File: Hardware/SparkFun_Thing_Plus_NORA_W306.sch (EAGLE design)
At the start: 76 parts, among them J1 THING_PLUS_LOGICAL, J2 LiPo, J3 QWIIC_RA, J4 MICRO-SDFRICTION, J5 USB-C, J6 SWD, Q1 3.1A/30V/105mΩ, Q2 MBT3904DW1T1, U1 UBLOX_NORA_W306, U3 XC6222B331MR-G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

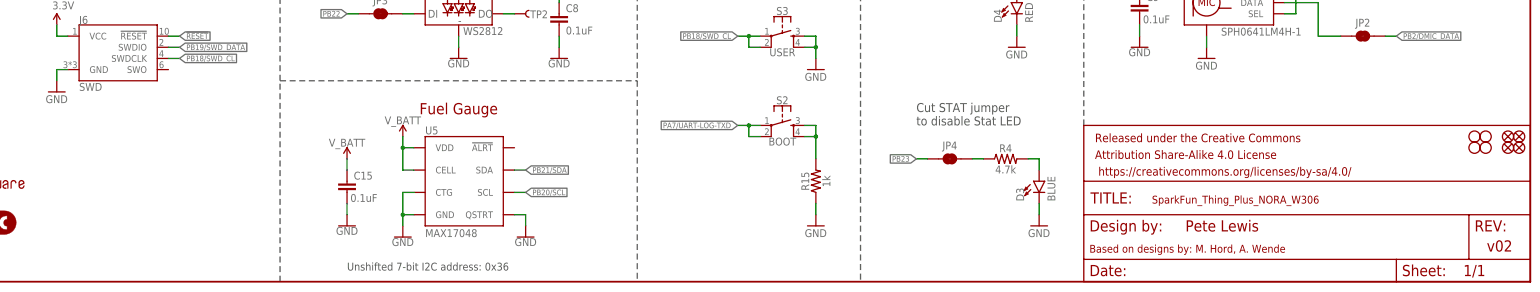
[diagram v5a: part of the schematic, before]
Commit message: SWD header to DNP and bumped version to v03
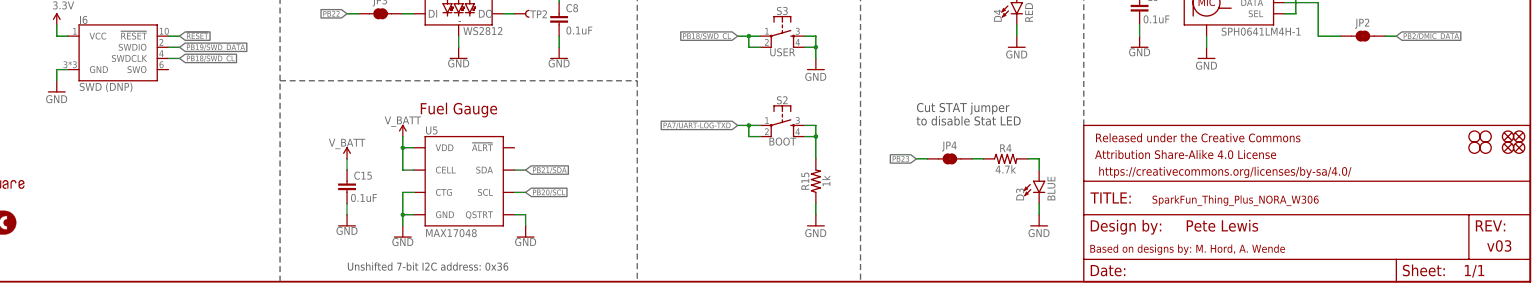
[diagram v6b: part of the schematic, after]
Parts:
- J6: value SWD -> SWD (DNP)
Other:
- note added: "v03"
- note removed: "v02"
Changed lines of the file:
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@@
 <part name="C11" library="SparkFun-Capacitors" deviceset="0.1UF" device="-0402T-16V-10%" value="0.1uF"/>
 <part name="GND7" library="SparkFun-PowerSymbols" deviceset="GND" device=""/>
-<part name="J6" library="SparkFun-Connectors" deviceset="CORTEX_JTAG_DEBUG_MINIMUM" device="_SMD-UNSHROUDED" value="SWD"/>
+<part name="J6" library="SparkFun-Connectors" deviceset="CORTEX_JTAG_DEBUG_MINIMUM" device="_SMD-UNSHROUDED" value="SWD (DNP)"/>
 <part name="SUPPLY31" library="SparkFun-PowerSymbols" deviceset="3.3V" device=""/>
 <part name="GND33" library="SparkFun-PowerSymbols" deviceset="GND" device=""/>
@@
 <text x="73.66" y="175.26" size="2.54" layer="94" font="vector" align="bottom-center">u-blox NORA-W306 Module</text>
 <text x="182.88" y="175.26" size="2.54" layer="94" font="vector" align="bottom-center">Thing Plus Headers</text>
-<text x="421.894" y="9.398" size="2.54" layer="94" font="vector" align="top-left">v02</text>
+<text x="421.894" y="9.398" size="2.54" layer="94" font="vector" align="top-left">v03</text>
 <text x="391.16" y="175.26" size="2.54" layer="94" font="vector" align="bottom-center">QWIIC Connector &amp; I2C Pullups</text>
 <text x="353.314" y="11.43" size="2.54" layer="94" font="vector">Pete Lewis</text>

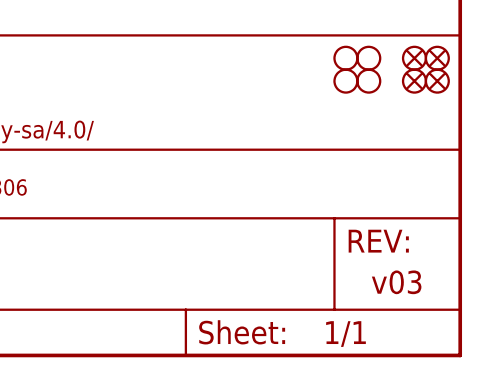
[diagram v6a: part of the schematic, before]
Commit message: removed paste from cortex debug SMD footprint (DNP)
-also bumped version to v04
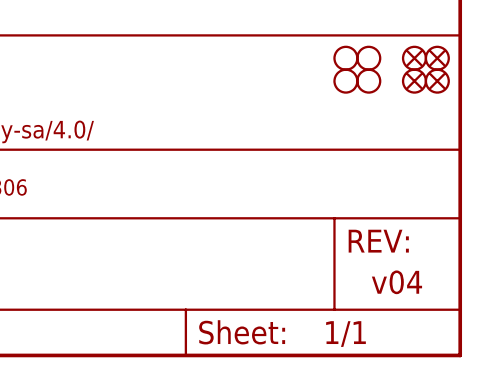
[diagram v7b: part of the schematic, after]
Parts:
- J6: device SparkFun-Connectors:CORTEX_JTAG_DEBUG_MINIMUM_SMD-UNSHROUDED -> SparkFun-Connectors:CORTEX_JTAG_DEBUG_MINIMUM_SMD_UNSHROUDED_DNP_NO_PASTE
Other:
- note added: "v04"
- note removed: "v03"
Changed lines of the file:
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@@
 <grid distance="0.1" unitdist="inch" unit="inch" style="lines" multiple="1" display="no" altdistance="0.01" altunitdist="inch" altunit="inch"/>
 <layers>
-<layer number="1" name="Top" color="4" fill="1" visible="no" active="no"/>
-<layer number="2" name="Route2" color="1" fill="3" visible="no" active="no"/>
-<layer number="3" name="Route3" color="4" fill="3" visible="no" active="no"/>
-<layer number="4" name="Route4" color="1" fill="4" visible="no" active="no"/>
-<layer number="5" name="Route5" color="4" fill="4" visible="no" active="no"/>
-<layer number="6" name="Route6" color="1" fill="8" visible="no" active="no"/>
-<layer number="7" name="Route7" color="4" fill="8" visible="no" active="no"/>
-<layer number="8" name="Route8" color="1" fill="2" visible="no" active="no"/>
-<layer number="9" name="Route9" color="4" fill="2" visible="no" active="no"/>
-<layer number="10" name="Route10" color="1" fill="7" visible="no" active="no"/>
-<layer number="11" name="Route11" color="4" fill="7" visible="no" active="no"/>
-<layer number="12" name="Route12" color="1" fill="5" visible="no" active="no"/>
-<layer number="13" name="Route13" color="4" fill="5" visible="no" active="no"/>
-<layer number="14" name="Route14" color="1" fill="6" visible="no" active="no"/>
-<layer number="15" name="Route15" color="11" fill="6" visible="no" active="no"/>
-<layer number="16" name="Bottom" color="1" fill="1" visible="no" active="no"/>
-<layer number="17" name="Pads" color="2" fill="1" visible="no" active="no"/>
-<layer number="18" name="Vias" color="2" fill="1" visible="no" active="no"/>
-<layer number="19" name="Unrouted" color="6" fill="1" visible="no" active="no"/>
-<layer number="20" name="Dimension" color="24" fill="1" visible="no" active="no"/>
-<layer number="21" name="tPlace" color="16" fill="1" visible="no" active="no"/>
-<layer number="22" name="bPlace" color="14" fill="1" visible="no" active="no"/>
-<layer number="23" name="tOrigins" color="15" fill="1" visible="no" active="no"/>
-<layer number="24" name="bOrigins" color="15" fill="1" visible="no" active="no"/>
-<layer number="25" name="tNames" color="7" fill="1" visible="no" active="no"/>
-<layer number="26" name="bNames" color="7" fill="1" visible="no" active="no"/>
-<layer number="27" name="tValues" color="7" fill="1" visible="no" active="no"/>
-<layer number="28" name="bValues" color="7" fill="1" visible="no" active="no"/>
+<layer number="1" name="Top" color="4" fill="1" visible="yes" active="no"/>
+<layer number="2" name="Route2" color="1" fill="3" visible="yes" active="no"/>
+<layer number="3" name="Route3" color="4" fill="3" visible="yes" active="no"/>
+<layer number="4" name="Route4" color="1" fill="4" visible="yes" active="no"/>
+<layer number="5" name="Route5" color="4" fill="4" visible="yes" active="no"/>
+<layer number="6" name="Route6" color="1" fill="8" visible="yes" active="no"/>
+<layer number="7" name="Route7" color="4" fill="8" visible="yes" active="no"/>
+<layer number="8" name="Route8" color="1" fill="2" visible="yes" active="no"/>
+<layer number="9" name="Route9" color="4" fill="2" visible="yes" active="no"/>
+<layer number="10" name="Route10" color="1" fill="7" visible="yes" active="no"/>
+<layer number="11" name="Route11" color="4" fill="7" visible="yes" active="no"/>
+<layer number="12" name="Route12" color="1" fill="5" visible="yes" active="no"/>
+<layer number="13" name="Route13" color="4" fill="5" visible="yes" active="no"/>
+<layer number="14" name="Route14" color="1" fill="6" visible="yes" active="no"/>
+<layer number="15" name="Route15" color="11" fill="6" visible="yes" active="no"/>
+<layer number="16" name="Bottom" color="1" fill="1" visible="yes" active="no"/>
+<layer number="17" name="Pads" color="2" fill="1" visible="yes" active="no"/>
+<layer number="18" name="Vias" color="2" fill="1" visible="yes" active="no"/>
+<layer number="19" name="Unrouted" color="6" fill="1" visible="yes" active="no"/>
+<layer number="20" name="Dimension" color="24" fill="1" visible="yes" active="no"/>
+<layer number="21" name="tPlace" color="16" fill="1" visible="yes" active="no"/>
+<layer number="22" name="bPlace" color="14" fill="1" visible="yes" active="no"/>
+<layer number="23" name="tOrigins" color="15" fill="1" visible="yes" active="no"/>
+<layer number="24" name="bOrigins" color="15" fill="1" visible="yes" active="no"/>
+<layer number="25" name="tNames" color="7" fill="1" visible="yes" active="no"/>
+<layer number="26" name="bNames" color="7" fill="1" visible="yes" active="no"/>
+<layer number="27" name="tValues" color="7" fill="1" visible="yes" active="no"/>
+<layer number="28" name="bValues" color="7" fill="1" visible="yes" active="no"/>
 <layer number="29" name="tStop" color="7" fill="3" visible="no" active="no"/>
 <layer number="30" name="bStop" color="7" fill="6" visible="no" active="no"/>
@@
 <layer number="35" name="tGlue" color="7" fill="4" visible="no" active="no"/>
 <layer number="36" name="bGlue" color="7" fill="5" visible="no" active="no"/>
-<layer number="37" name="tTest" color="7" fill="1" visible="no" active="no"/>
-<layer number="38" name="bTest" color="7" fill="1" visible="no" active="no"/>
+<layer number="37" name="tTest" color="7" fill="1" visible="yes" active="no"/>
+<layer number="38" name="bTest" color="7" fill="1" visible="yes" active="no"/>
 <layer number="39" name="tKeepout" color="4" fill="11" visible="no" active="no"/>
 <layer number="40" name="bKeepout" color="1" fill="11" visible="no" active="no"/>
@@
 <layer number="44" name="Drills" color="7" fill="1" visible="no" active="no"/>
 <layer number="45" name="Holes" color="7" fill="1" visible="no" active="no"/>
-<layer number="46" name="Milling" color="3" fill="1" visible="no" active="no"/>
-<layer number="47" name="Measures" color="7" fill="1" visible="no" active="no"/>
-<layer number="48" name="Document" color="7" fill="1" visible="no" active="no"/>
-<layer number="49" name="Reference" color="7" fill="1" visible="no" active="no"/>
-<layer number="50" name="dxf" color="7" fill="1" visible="no" active="no"/>
-<layer number="51" name="tDocu" color="6" fill="1" visible="no" active="no"/>
-<layer number="52" name="bDocu" color="7" fill="1" visible="no" active="no"/>
-<layer number="53" name="tGND_GNDA" color="7" fill="9" visible="no" active="no"/>
-<layer number="54" name="bGND_GNDA" color="1" fill="9" visible="no" active="no"/>
-<layer number="56" name="wert" color="7" fill="1" visible="no" active="no"/>
-<layer number="57" name="tCAD" color="7" fill="1" visible="no" active="no"/>
-<layer number="58" name="bCopper" color="7" fill="1" visible="no" active="no"/>
-<layer number="59" name="tCarbon" color="7" fill="1" visible="no" active="no"/>
-<layer number="60" name="bCarbon" color="7" fill="1" visible="no" active="no"/>
+<layer number="46" name="Milling" color="3" fill="1" visible="yes" active="no"/>
+<layer number="47" name="Measures" color="7" fill="1" visible="yes" active="no"/>
+<layer number="48" name="Document" color="7" fill="1" visible="yes" active="no"/>
+<layer number="49" name="Reference" color="7" fill="1" visible="yes" active="no"/>
+<layer number="50" name="dxf" color="7" fill="1" visible="yes" active="no"/>
+<layer number="51" name="tDocu" color="6" fill="1" visible="yes" active="no"/>
+<layer number="52" name="bDocu" color="7" fill="1" visible="yes" active="no"/>
+<layer number="53" name="tGND_GNDA" color="7" fill="9" visible="yes" active="no"/>
+<layer number="54" name="bGND_GNDA" color="1" fill="9" visible="yes" active="no"/>
+<layer number="56" name="wert" color="7" fill="1" visible="yes" active="no"/>
+<layer number="57" name="tCAD" color="7" fill="1" visible="yes" active="no"/>
+<layer number="58" name="bCopper" color="7" fill="1" visible="yes" active="no"/>
+<layer number="59" name="tCarbon" color="7" fill="1" visible="yes" active="no"/>
+<layer number="60" name="bCarbon" color="7" fill="1" visible="yes" active="no"/>
 <layer number="88" name="SimResults" color="9" fill="1" visible="yes" active="yes"/>
 <layer number="89" name="SimProbes" color="9" fill="1" visible="yes" active="yes"/>
@@
 <part name="C11" library="SparkFun-Capacitors" deviceset="0.1UF" device="-0402T-16V-10%" value="0.1uF"/>
 <part name="GND7" library="SparkFun-PowerSymbols" deviceset="GND" device=""/>
-<part name="J6" library="SparkFun-Connectors" deviceset="CORTEX_JTAG_DEBUG_MINIMUM" device="_SMD-UNSHROUDED" value="SWD (DNP)"/>
+<part name="J6" library="SparkFun-Connectors" deviceset="CORTEX_JTAG_DEBUG_MINIMUM" device="_SMD_UNSHROUDED_DNP_NO_PASTE" value="SWD (DNP)"/>
 <part name="SUPPLY31" library="SparkFun-PowerSymbols" deviceset="3.3V" device=""/>
 <part name="GND33" library="SparkFun-PowerSymbols" deviceset="GND" device=""/>
@@
 <text x="73.66" y="175.26" size="2.54" layer="94" font="vector" align="bottom-center">u-blox NORA-W306 Module</text>
 <text x="182.88" y="175.26" size="2.54" layer="94" font="vector" align="bottom-center">Thing Plus Headers</text>
-<text x="421.894" y="9.398" size="2.54" layer="94" font="vector" align="top-left">v03</text>
+<text x="421.894" y="9.398" size="2.54" layer="94" font="vector" align="top-left">v04</text>
 <text x="391.16" y="175.26" size="2.54" layer="94" font="vector" align="bottom-center">QWIIC Connector &amp; I2C Pullups</text>
 <text x="353.314" y="11.43" size="2.54" layer="94" font="vector">Pete Lewis</text>

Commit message: Correcting SWD_DATA and SWD_CLK
-In the Symbol Pin names, Removed SWD DATA and CL from PB18/PB19
-Removed PDM mic
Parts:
- removed C9: 0.1uF, SparkFun-Capacitors:0.1UF-0402T-16V-10%
- removed E1: SPH0641LM4H-1, SparkFun-Sensors:SPH0641LM4H-1_MICROPHONE
- removed JP1, JP2: JUMPER-SMT_2_NC_TRACE_SILK, SparkFun-Jumpers:JUMPER-SMT_2_NC_TRACE_SILK
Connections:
- removed net N$29: E1.DATA, JP2.1
- removed net N$30: E1.CLK, JP1.1
- removed net PA27: J1.FREEBIE, U1.PA27/SWD_DATA/LP_UART_RTS/WLAN_ACT
- removed net PB1/ADC/DMIC_CLK: J1.A0, JP1.2, U1.PB1/LP_UART_TXD/DMIC_CLK/ADC
- removed net PB18/SWD_CL: J1.GPIO3, J6.SWDCLK, S3.1, S3.2, U1.PB18/HS_USI_USART0_RXD/SWD_CL
- removed net PB19/SWD_DATA: J1.GPIO4, J6.SWDIO, U1.PB19/HS_UART0_TXD/SWD_DATA/I2S_TX0
- removed net PB2/DMIC_DATA: J1.A2, JP2.2, U1.PB2/LP_UART_RXD/PCM_CLK/DMIC_DATA/ADC
- removed net PB3/ADC: J1.A1, U1.PB3/SWD_CLK/ADC
- new net PA27/SWD_DATA: J1.FREEBIE, J6.SWDIO, U1.PA27/SWD_DATA/LP_UART_RTS/WLAN_ACT
- new net PB1: J1.A0, U1.PB1/LP_UART_TXD/ADC
- new net PB18: J1.GPIO3, S3.1, S3.2, U1.PB18/HS_USI_USART0_RXD
- new net PB19: J1.GPIO4, U1.PB19/HS_UART0_TXD/I2S_TX0
- new net PB2: J1.A2, U1.PB2/LP_UART_RXD/PCM_CLK/ADC
- new net PB3/ADC/SWD_CLK: J1.A1, J6.SWDCLK, U1.PB3/SWD_CLK/ADC
- net 3.3V: no longer C9.1, E1.SEL, E1.VDD
- net GND: no longer C9.2, E1.GND
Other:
- note removed: "Cut JP1 and JP2 To disconnect MIC from A2 and A0"
- note removed: "Microphone"
